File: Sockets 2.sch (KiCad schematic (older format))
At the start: 67 parts, among them J21 TABLE SENSOR, J22 INPUT1, J23 INPUT2, J24 PHOTO SENSOR EMITER, J25 PHOTO SENSOR RECEIVER, J26 ANALOG, J27 INPUT3, J28 OUT1, J29 OUT2, J30 RELAY, Q10 2N7002K, Q11 BC817, Q12 BC817, Q13 BC817, Q14 2N7002K, Q15 2N7002K, Q16 2N7002K, Q9 2N7002K, U9 MCP6002-xSN

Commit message: Rozmieszczenie elementów, trasowanie ścieżek, etap 2/4
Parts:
- added C84: 0.1uF, Capacitor_SMD:C_0603_1608Metric, symbol Device:C_Small
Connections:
- net GNDA: now also C84.2
- net VDDA: now also C84.1
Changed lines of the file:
@@
 	7100 5000 7100 5100
 Wire Wire Line
-	7100 4400 7100 4200
+	7100 4400 7100 4250
 Wire Wire Line
 	7600 5950 7850 5950
@@
 	0    1    1    0
 $EndComp
+$Comp
+L Device:C_Small C?
+U 1 1 5E32152F
+P 6800 4350
+AR Path="/5DFB2EC0/5E32152F" Ref="C?"  Part="1"
+AR Path="/5E858220/5E32152F" Ref="C84"  Part="1"
+F 0 "C84" H 6900 4400 50  0000 L CNN
+F 1 "0.1uF" H 6900 4300 50  0000 L CNN
+F 2 "Capacitor_SMD:C_0603_1608Metric" H 6800 4350 50  0001 C CNN
+F 3 "~" H 6800 4350 50  0001 C CNN
+F 4 "0.05982" H 6800 4350 50  0001 C CNN "Cena"
+F 5 "CL10B104KB8NNNC " H 6800 4350 50  0001 C CNN "Model"
+F 6 "50V" H 6800 4350 50  0001 C CNN "Napięcie"
+F 7 "SAMSUNG" H 6800 4350 50  0001 C CNN "Producent"
+F 8 "10%" H 6800 4350 50  0001 C CNN "Tolerancja"
+F 9 "SMD" H 6800 4350 50  0001 C CNN "Typ"
+	1    6800 4350
+	1    0    0    -1
+$EndComp
+Wire Wire Line
+	6800 4250 7100 4250
+Connection ~ 7100 4250
+Wire Wire Line
+	7100 4250 7100 4200
+$Comp
+L power:GNDA #PWR0215
+U 1 1 5E33D1ED
+P 6800 4450
+F 0 "#PWR0215" H 6800 4200 50  0001 C CNN
+F 1 "GNDA" H 6805 4277 50  0000 C CNN
+F 2 "" H 6800 4450 50  0001 C CNN
+F 3 "" H 6800 4450 50  0001 C CNN
+	1    6800 4450
+	1    0    0    -1
+$EndComp
 $EndSCHEMATC

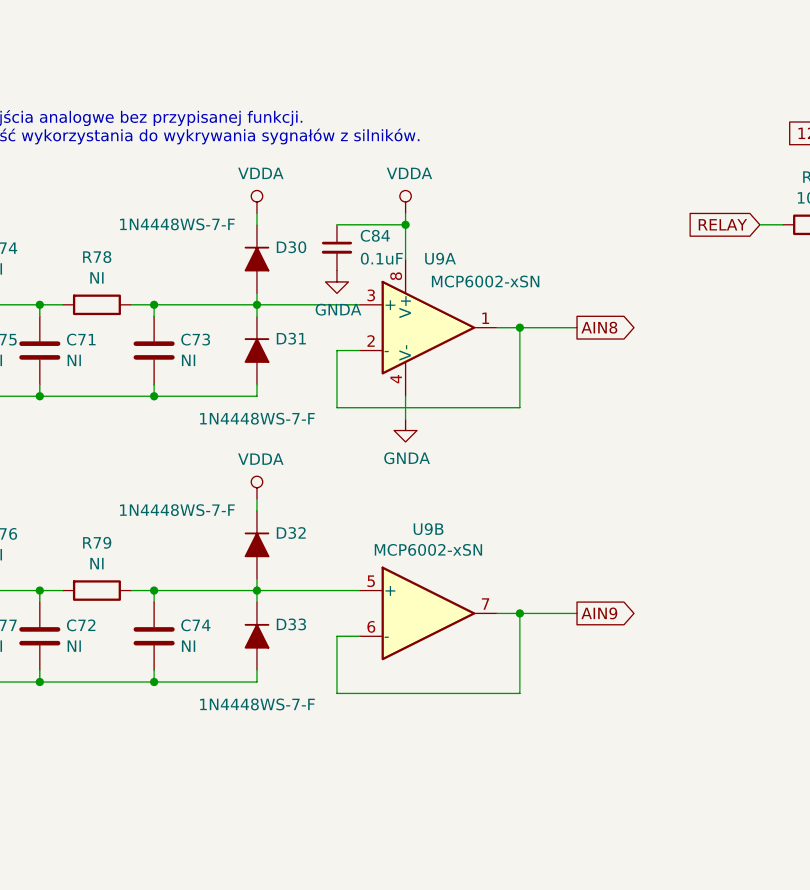
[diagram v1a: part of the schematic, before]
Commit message: Test points, start power plane routing, little change on schematic
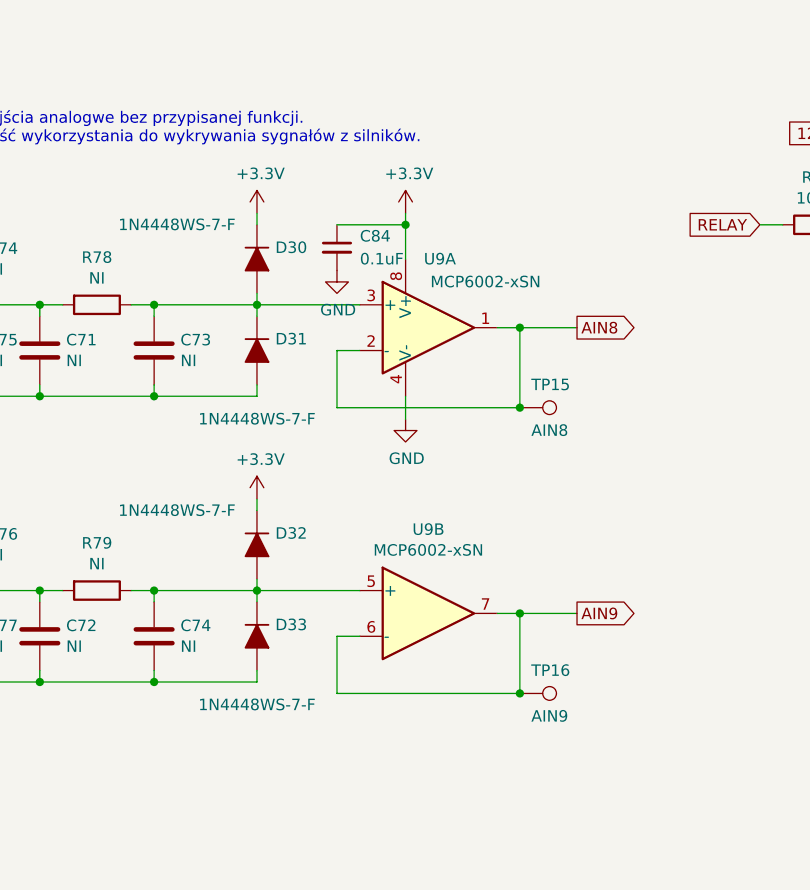
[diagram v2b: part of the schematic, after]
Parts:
- added TP15: AIN8, TestPoint:TestPoint_Pad_D1.5mm, symbol Connector:TestPoint
- added TP16: AIN9, TestPoint:TestPoint_Pad_D1.5mm, symbol Connector:TestPoint
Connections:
- net GNDA is gone; now on net GND: C84.2, U9.4 (V-)
- net VDDA is gone; now on net +3V3: C84.1, D30.1 (K), D32.1 (K), U9.8 (V+)
- net AIN8: now also TP15.1
- net AIN9: now also TP16.1
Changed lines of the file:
@@
 Wire Wire Line
 	6450 4200 6450 4250
-$Comp
-L power:VDDA #PWR?
-U 1 1 5E2765FE
-P 6450 4200
-AR Path="/5DFB2EC0/5E2765FE" Ref="#PWR?"  Part="1"
-AR Path="/5E858220/5E2765FE" Ref="#PWR0164"  Part="1"
-F 0 "#PWR0164" H 6450 4050 50  0001 C CNN
-F 1 "VDDA" H 6467 4373 50  0000 C CNN
-F 2 "" H 6450 4200 50  0001 C CNN
-F 3 "" H 6450 4200 50  0001 C CNN
-	1    6450 4200
-	1    0    0    -1
-$EndComp
 Wire Wire Line
 	6000 5000 5500 5000
@@
 Wire Wire Line
 	6450 5450 6450 5500
-$Comp
-L power:VDDA #PWR?
-U 1 1 5E29E60D
-P 6450 5450
-AR Path="/5DFB2EC0/5E29E60D" Ref="#PWR?"  Part="1"
-AR Path="/5E858220/5E29E60D" Ref="#PWR0165"  Part="1"
-F 0 "#PWR0165" H 6450 5300 50  0001 C CNN
-F 1 "VDDA" H 6467 5623 50  0000 C CNN
-F 2 "" H 6450 5450 50  0001 C CNN
-F 3 "" H 6450 5450 50  0001 C CNN
-	1    6450 5450
-	1    0    0    -1
-$EndComp
 Wire Wire Line
 	6000 6250 5500 6250
@@
 Wire Wire Line
 	4850 4500 4850 6250
-$Comp
-L power:GNDA #PWR0169
-U 1 1 5E2F66C6
-P 7100 5100
-F 0 "#PWR0169" H 7100 4850 50  0001 C CNN
-F 1 "GNDA" H 7105 4927 50  0000 C CNN
-F 2 "" H 7100 5100 50  0001 C CNN
-F 3 "" H 7100 5100 50  0001 C CNN
-	1    7100 5100
-	1    0    0    -1
-$EndComp
-$Comp
-L power:VDDA #PWR?
-U 1 1 5E2F75E8
-P 7100 4200
-AR Path="/5DFB2EC0/5E2F75E8" Ref="#PWR?"  Part="1"
-AR Path="/5E858220/5E2F75E8" Ref="#PWR0168"  Part="1"
-F 0 "#PWR0168" H 7100 4050 50  0001 C CNN
-F 1 "VDDA" H 7117 4373 50  0000 C CNN
-F 2 "" H 7100 4200 50  0001 C CNN
-F 3 "" H 7100 4200 50  0001 C CNN
-	1    7100 4200
-	1    0    0    -1
-$EndComp
 Wire Wire Line
 	7100 5000 7100 5100
@@
 	7100 4250 7100 4200
 $Comp
-L power:GNDA #PWR0215
-U 1 1 5E33D1ED
+L Connector:TestPoint TP?
+U 1 1 5E324927
+P 7600 5050
+AR Path="/5DE588DC/5E324927" Ref="TP?"  Part="1"
+AR Path="/5DE587B9/5E324927" Ref="TP?"  Part="1"
+AR Path="/5E1018C2/5E324927" Ref="TP?"  Part="1"
+AR Path="/5DFB2EC0/5E324927" Ref="TP?"  Part="1"
+AR Path="/5E858220/5E324927" Ref="TP15"  Part="1"
+F 0 "TP15" V 7500 5100 50  0000 L CNN
+F 1 "AIN8" V 7700 5100 50  0000 L CNN
+F 2 "TestPoint:TestPoint_Pad_D1.5mm" H 7800 5050 50  0001 C CNN
+F 3 "~" H 7800 5050 50  0001 C CNN
+	1    7600 5050
+	0    1    1    0
+$EndComp
+$Comp
+L Connector:TestPoint TP?
+U 1 1 5E331E87
+P 7600 6300
+AR Path="/5DE588DC/5E331E87" Ref="TP?"  Part="1"
+AR Path="/5DE587B9/5E331E87" Ref="TP?"  Part="1"
+AR Path="/5E1018C2/5E331E87" Ref="TP?"  Part="1"
+AR Path="/5DFB2EC0/5E331E87" Ref="TP?"  Part="1"
+AR Path="/5E858220/5E331E87" Ref="TP16"  Part="1"
+F 0 "TP16" V 7500 6350 50  0000 L CNN
+F 1 "AIN9" V 7700 6350 50  0000 L CNN
+F 2 "TestPoint:TestPoint_Pad_D1.5mm" H 7800 6300 50  0001 C CNN
+F 3 "~" H 7800 6300 50  0001 C CNN
+	1    7600 6300
+	0    1    1    0
+$EndComp
+Connection ~ 7600 5050
+Connection ~ 7600 6300
+$Comp
+L power:GND #PWR?
+U 1 1 5E492E79
+P 7100 5100
+AR Path="/5E07245F/5E492E79" Ref="#PWR?"  Part="1"
+AR Path="/5E858220/5E492E79" Ref="#PWR0110"  Part="1"
+F 0 "#PWR0110" H 7100 4850 50  0001 C CNN
+F 1 "GND" H 7105 4927 50  0000 C CNN
+F 2 "" H 7100 5100 50  0001 C CNN
+F 3 "" H 7100 5100 50  0001 C CNN
+	1    7100 5100
+	1    0    0    -1
+$EndComp
+$Comp
+L power:+3.3V #PWR0111
+U 1 1 5E4934D3
+P 6450 4200
+F 0 "#PWR0111" H 6450 4050 50  0001 C CNN
+F 1 "+3.3V" H 6465 4373 50  0000 C CNN
+F 2 "" H 6450 4200 50  0001 C CNN
+F 3 "" H 6450 4200 50  0001 C CNN
+	1    6450 4200
+	1    0    0    -1
+$EndComp
+$Comp
+L power:+3.3V #PWR0164
+U 1 1 5E493DB1
+P 6450 5450
+F 0 "#PWR0164" H 6450 5300 50  0001 C CNN
+F 1 "+3.3V" H 6465 5623 50  0000 C CNN
+F 2 "" H 6450 5450 50  0001 C CNN
+F 3 "" H 6450 5450 50  0001 C CNN
+	1    6450 5450
+	1    0    0    -1
+$EndComp
+$Comp
+L power:+3.3V #PWR0165
+U 1 1 5E496034
+P 7100 4200
+F 0 "#PWR0165" H 7100 4050 50  0001 C CNN
+F 1 "+3.3V" H 7115 4373 50  0000 C CNN
+F 2 "" H 7100 4200 50  0001 C CNN
+F 3 "" H 7100 4200 50  0001 C CNN
+	1    7100 4200
+	1    0    0    -1
+$EndComp
+$Comp
+L power:GND #PWR?
+U 1 1 5E499248
 P 6800 4450
-F 0 "#PWR0215" H 6800 4200 50  0001 C CNN
-F 1 "GNDA" H 6805 4277 50  0000 C CNN
+AR Path="/5E07245F/5E499248" Ref="#PWR?"  Part="1"
+AR Path="/5E858220/5E499248" Ref="#PWR0169"  Part="1"
+F 0 "#PWR0169" H 6800 4200 50  0001 C CNN
+F 1 "GND" H 6805 4277 50  0000 C CNN
 F 2 "" H 6800 4450 50  0001 C CNN
 F 3 "" H 6800 4450 50  0001 C CNN

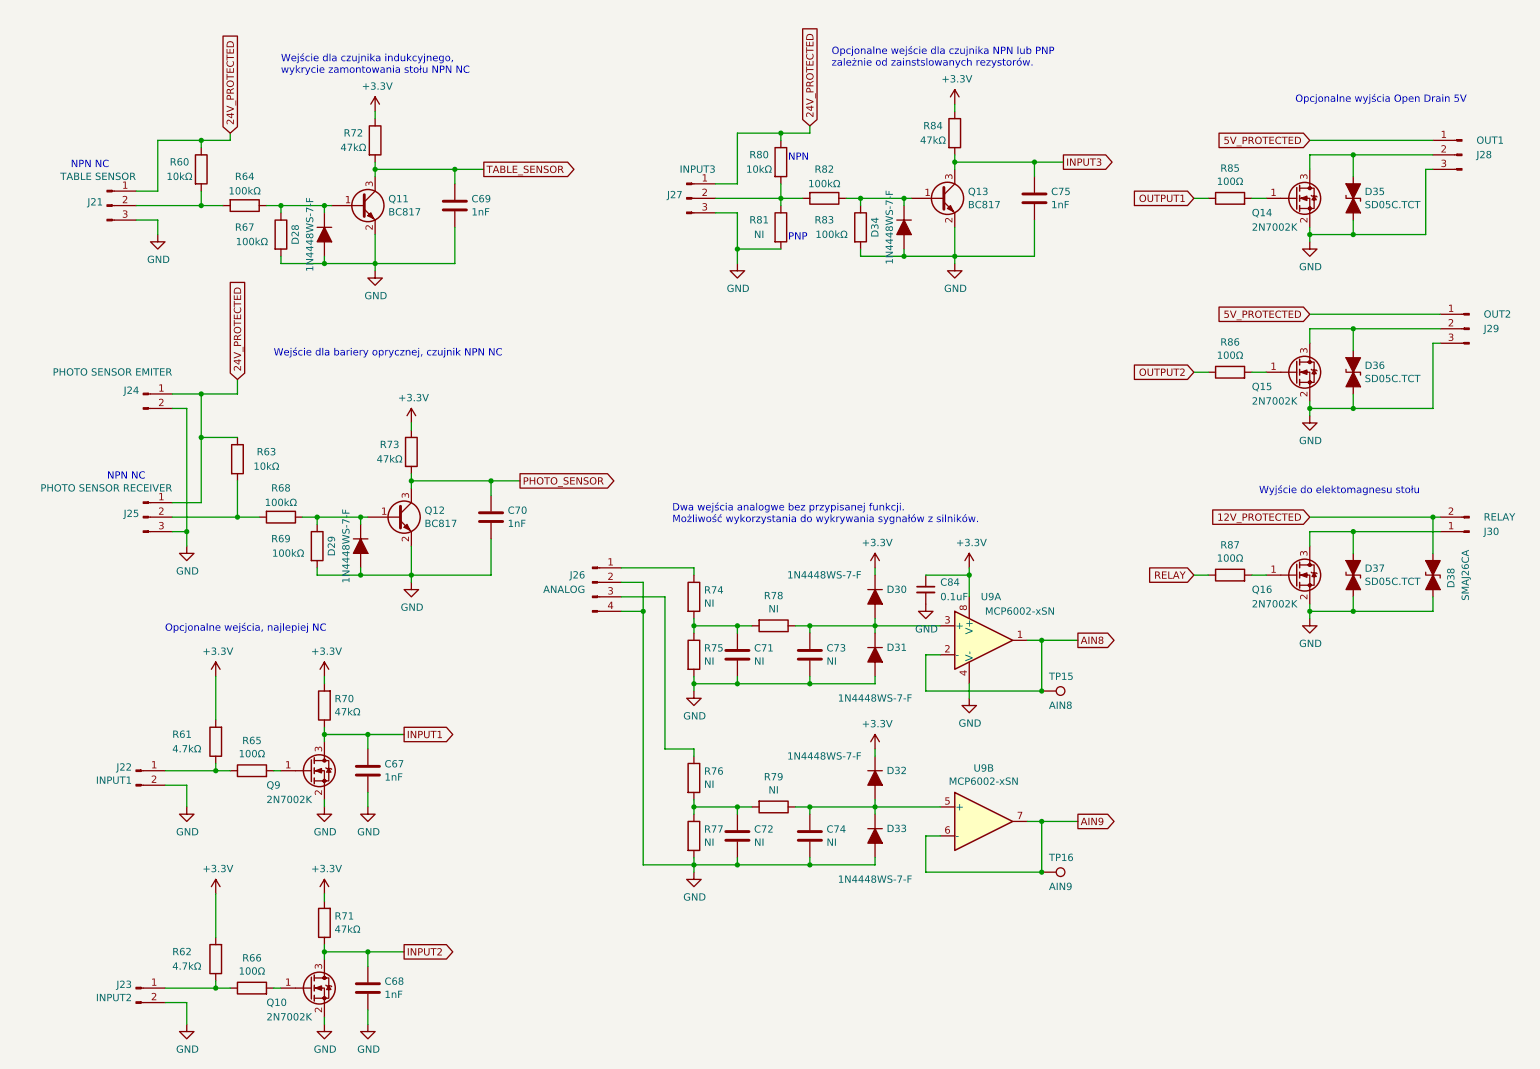
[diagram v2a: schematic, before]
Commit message: Update elements value
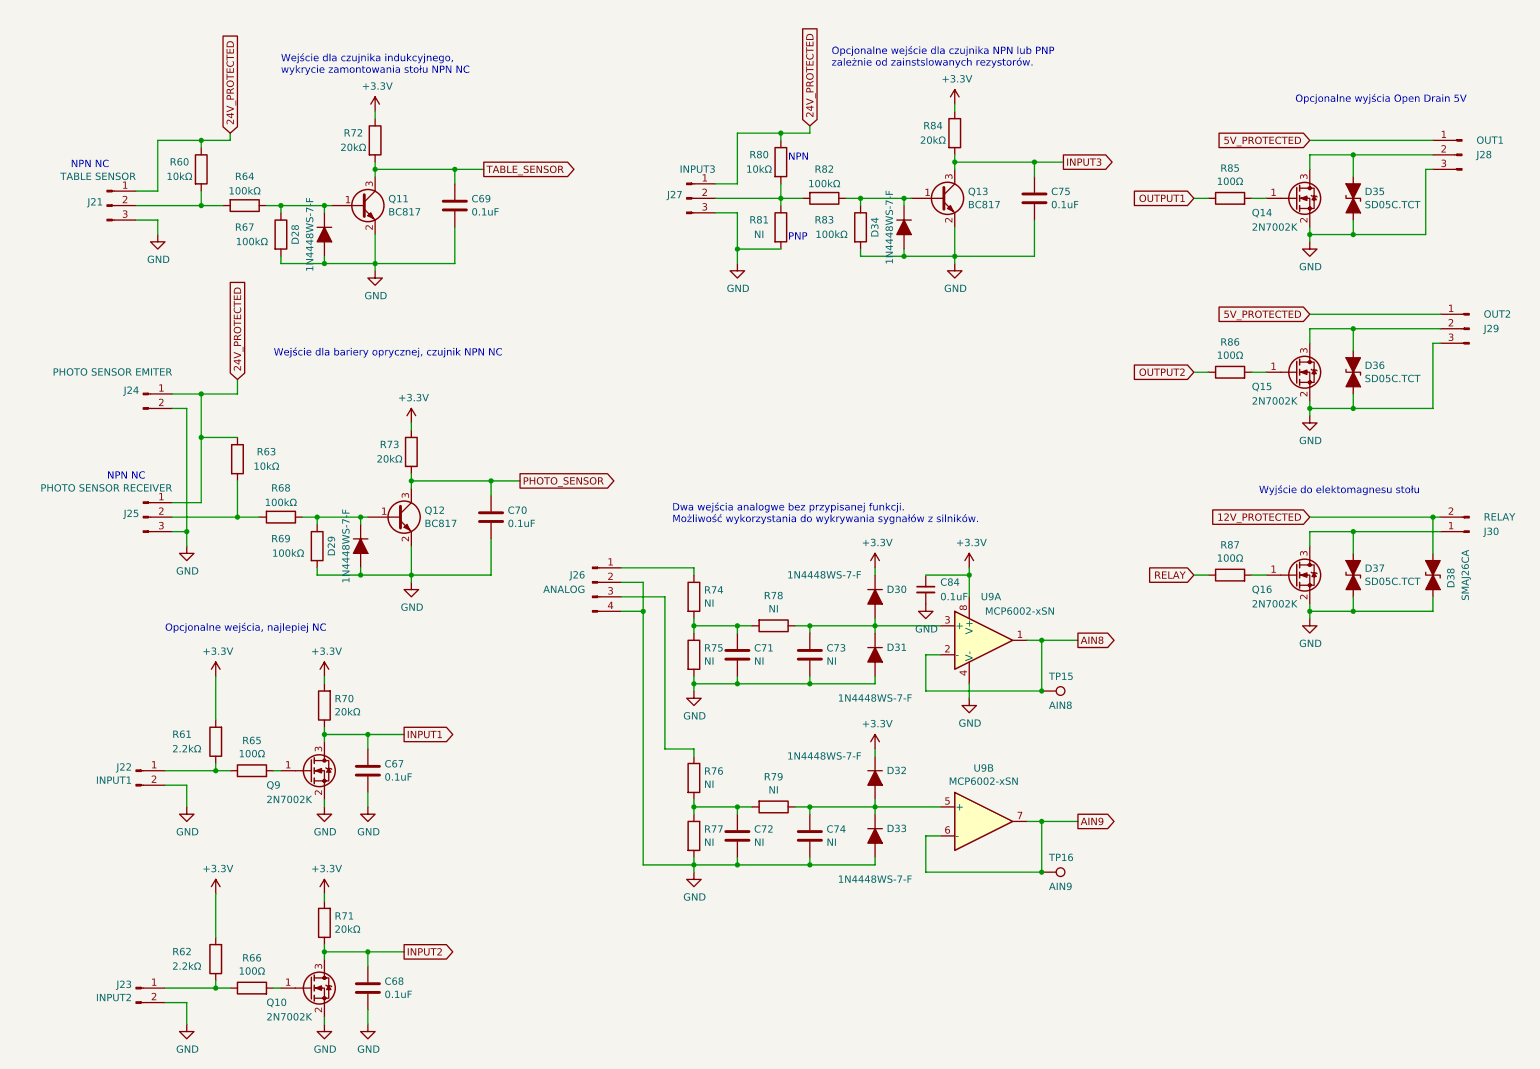
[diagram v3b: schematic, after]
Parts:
- C67, C68, C69, C70, C75: value 1nF -> 0.1uF
- C71, C72, C73, C74, R74, R75, R76, R77, R78, R79: Typ (none) -> SMD
- R61, R62: value 4.7kΩ -> 2.2kΩ
- R65, R66, R85, R86, R87: Cena (none) -> 0.03185; Link (none) -> https://www.tme.eu/pl/details/smd0603-100r-1%25/rezystory-s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; Model (none) -> 0603SAF1000T5E; Opis (none) -> Rezystor: thick film; SMD; 0603; 100Ω; 0,1W; ±1%; -55÷155°C; Producent (none) -> ROYAL OHM; Typ (none) -> SMD
- R70, R71: value 47kΩ -> 20kΩ; Cena (none) -> 0.03572; Link (none) -> https://www.tme.eu/pl/details/smd0603-47k/rezystory-smd-060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; Model (none) -> 0603SAJ0473T5E; Opis (none) -> Rezystor: thick film; SMD; 0603; 47kΩ; 0,1W; ±5%; -55÷155°C; Producent (none) -> ROYAL OHM; Typ (none) -> SMD
- R72, R73, R84: value 47kΩ -> 20kΩ; Cena 0.03622 -> 0.03572; Link https://www.tme.eu/pl/details/smd0603-10k-1%25/rezystory-sm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 -> https://www.tme.eu/pl/details/smd0603-47k/rezystory-smd-060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; Model 0603SAF1002T5E -> 0603SAJ0473T5E; Opis Rezystor: thick film; SMD; 0603; 10kΩ; 0,1W; ±1%; -55÷155°C -> Rezystor: thick film; SMD; 0603; 47kΩ; 0,1W; ±5%; -55÷155°C
- R81: Cena 0.03622 -> (none); Link https://www.tme.eu/pl/details/smd0603-10k-1%25/rezystory-sm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 -> (none); Model 0603SAF1002T5E -> (none); Opis Rezystor: thick film; SMD; 0603; 10kΩ; 0,1W; ±1%; -55÷155°C -> (none); Producent ROYAL OHM -> (none)
- U9: Cena (none) -> 2.07; Link (none) -> https://www.tme.eu/pl/details/mcp6002t-i_sn/wzmacniacze-ope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; Model (none) -> MCP6002T-I/SN; Opis (none) -> Wzmacniacz operacyjny; 1MHz; 1,8÷5,5V; Kanały: 2; SO8; Producent (none) -> MICROCHIP; Typ (none) -> SMD
